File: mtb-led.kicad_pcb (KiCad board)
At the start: 2 copper layers, 120 x 50 mm, 60 parts, among them J7 AVR-ISP-6, J9 DEBUG, SW1 SW_Push, U1 ATmega328PB-A, U2 78M05, U3 TLC5940PWP, U4 TLC5940PWP, U5 MAX487E, Y1 14.7456 MHz

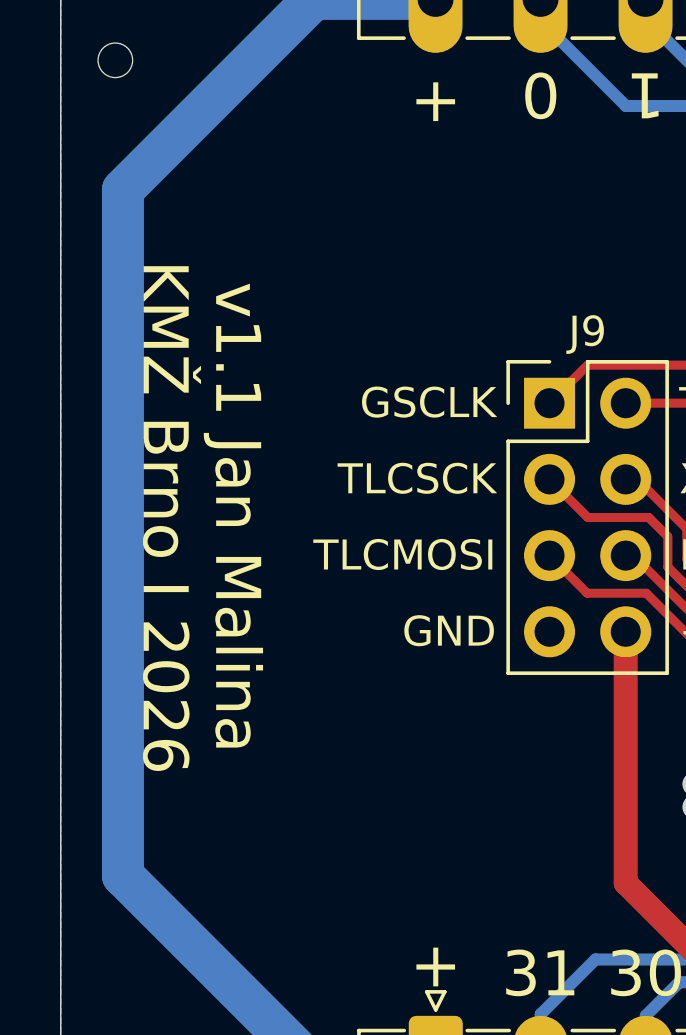
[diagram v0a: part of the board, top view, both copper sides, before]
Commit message: Sch: add I2C interface to ambient light sensor.
E.g. BH1750.
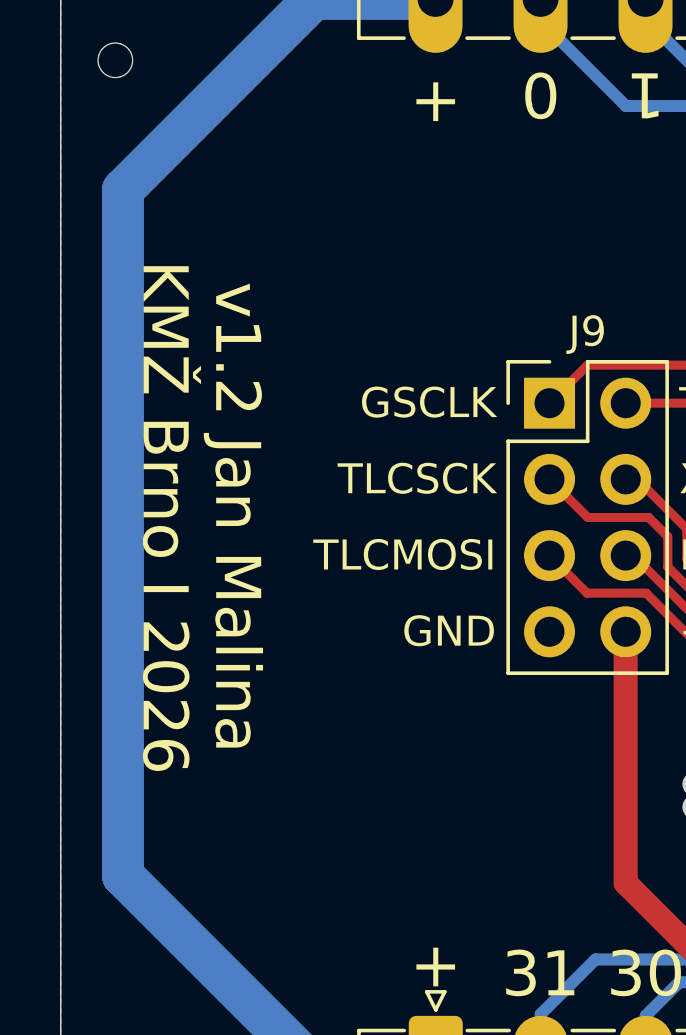
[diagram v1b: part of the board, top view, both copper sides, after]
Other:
- board text added: "v1.2 Jan Malina KMŽ Brno I 2026"
- board text removed: "v1.1 Jan Malina KMŽ Brno I 2026"
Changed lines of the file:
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@@
 		)
 	)
-	(gr_text "v1.1 Jan Malina\nKMŽ Brno I 2026"
+	(gr_text "v1.2 Jan Malina\nKMŽ Brno I 2026"
 		(at 84.582 94.488 270)
 		(layer "F.SilkS")

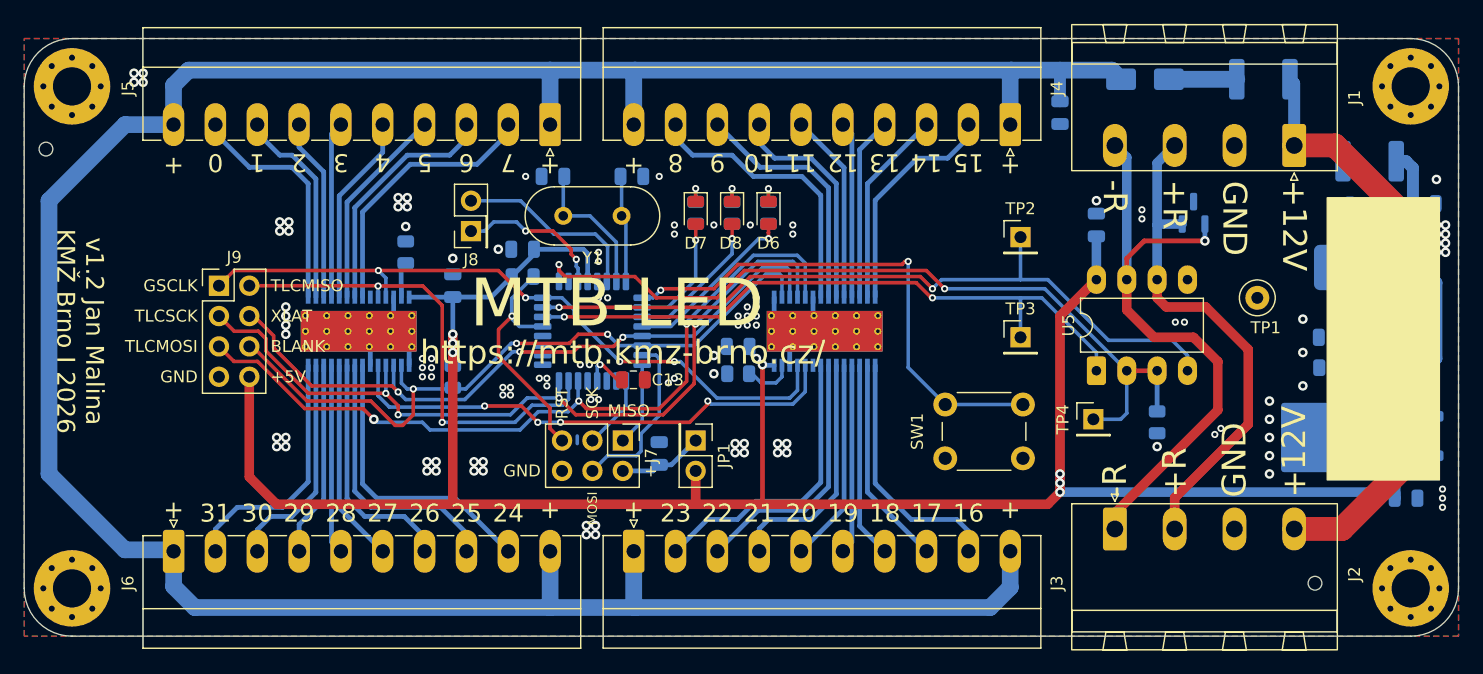
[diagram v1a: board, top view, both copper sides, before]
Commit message: PCB: wire light sensor connection.
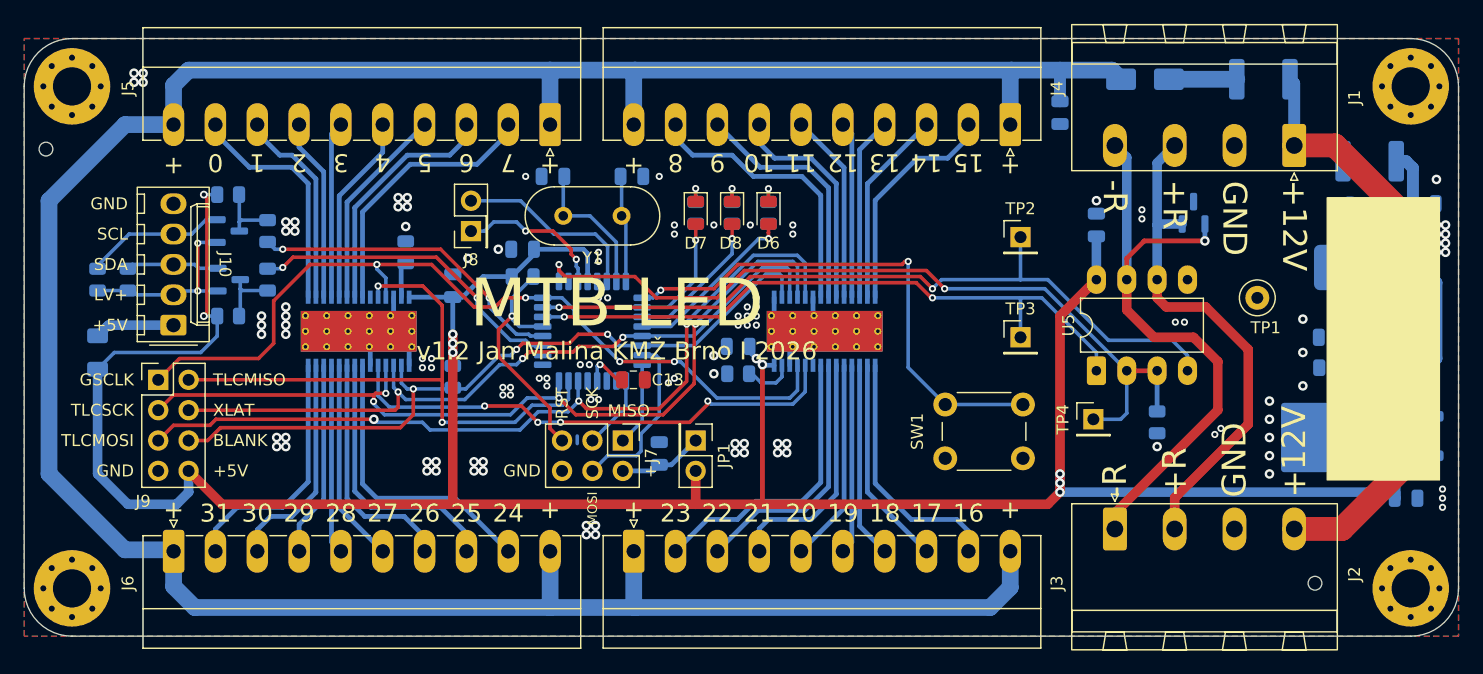
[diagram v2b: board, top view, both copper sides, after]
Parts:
- added F3: 50/100mA, Fuse:Fuse_1206_3216Metric, B.Cu at (88.1, 96.3)
- added J10: KK-254, Connector_Molex:Molex_KK-254_AE-6410-05A_1x05_P2.54mm_Vertical, F.Cu at (94.5, 94.0)
- added Q1: AO3400/BSS138, Package_TO_SOT_SMD:SOT-23, B.Cu at (99.1, 86.1)
- added Q2: AO3400/BSS138, Package_TO_SOT_SMD:SOT-23, B.Cu at (99.1, 90.2)
- added R11: 1k, Resistor_SMD:R_0805_2012Metric, B.Cu at (102.4, 86.1)
- added R12: 10k, Resistor_SMD:R_0805_2012Metric, B.Cu at (99.1, 93.2)
- added R13: 10k, Resistor_SMD:R_0805_2012Metric, B.Cu at (99.1, 83.1)
- added R14: 10k, Resistor_SMD:R_0805_2012Metric, B.Cu at (90.7, 90.2)
- added R15: 10k, Resistor_SMD:R_0805_2012Metric, B.Cu at (88.1, 90.2)
- added R9: 1k, Resistor_SMD:R_0805_2012Metric, B.Cu at (102.4, 90.2)
- JP1: value Jumper_2_Open -> ~
- moved J9 9.37 mm to (93.2, 98.6)
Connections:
- U1 pad 27: unconnected-(U1-PC4-Pad27) -> /SDA
- U1 pad 28: unconnected-(U1-PC5-Pad28) -> /SCL
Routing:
- net +5V: track 195.1 -> 237.0 mm, vias 8 -> 10
- net /SDA: track 0.00 -> 26.9 mm, vias 0 -> 2
- net /SCL: track 0.00 -> 26.8 mm, vias 0 -> 2
- net /LV+: track 0.00 -> 16.2 mm, vias 0 -> 2
- net /GSCLK: track 58.5 -> 70.5 mm
- net /LSCL: track 0.00 -> 11.9 mm
- net /TLCMISO: track 40.4 -> 50.9 mm
- net /LSDA: track 0.00 -> 7.80 mm
- net Net-(J10-Pin_1): track 0.00 -> 6.72 mm
- net Net-(Q1-D): track 0.00 -> 5.49 mm
- net Net-(Q2-D): track 0.00 -> 5.44 mm
- net /TLCSCK: track 68.7 -> 72.1 mm
- net /TLCMOSI: track 66.2 -> 69.5 mm
- net /XLAT: track 58.1 -> 61.2 mm
- net /BLANK: track 59.1 -> 62.0 mm
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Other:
- board text added: "LV+"
- board text added: "SCL"
- board text added: "SDA"
- board text removed: "https://mtb.kmz-brno.cz/"

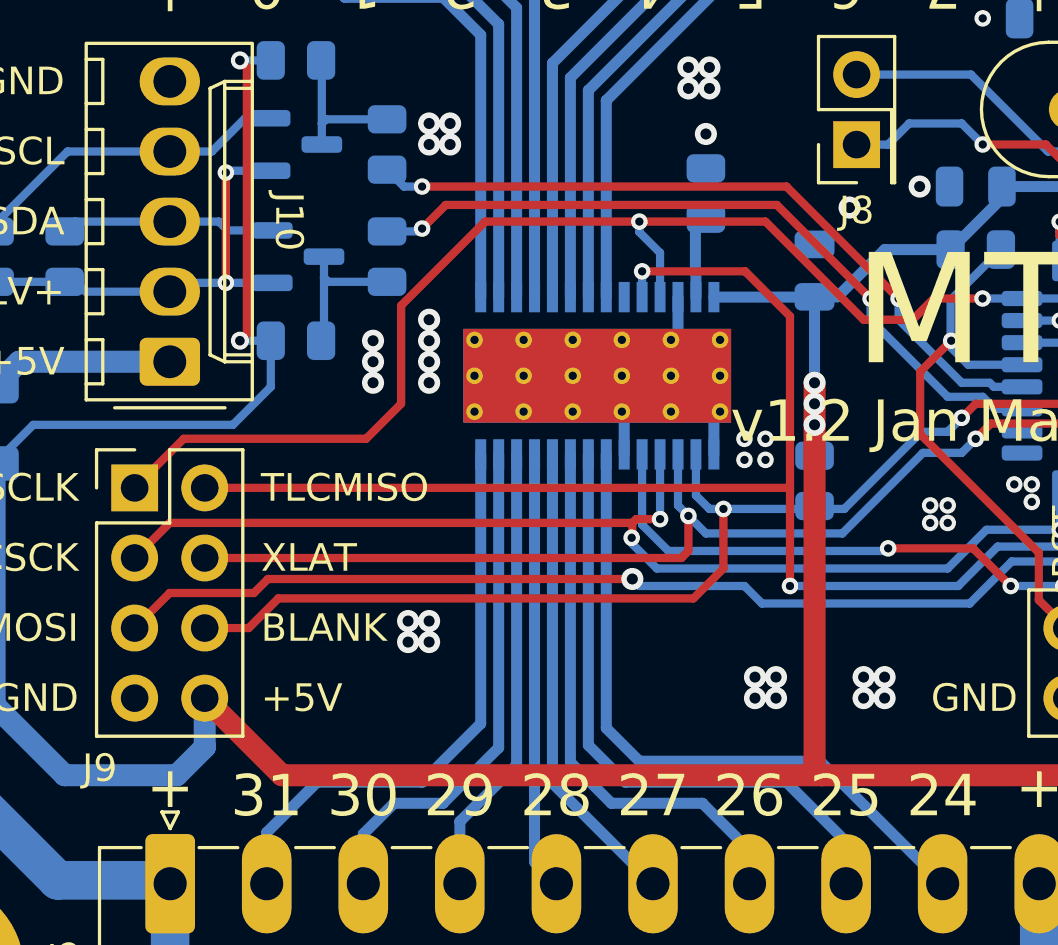
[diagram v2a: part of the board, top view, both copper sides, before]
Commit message: Enhance thermal conductivity from TLC5940.
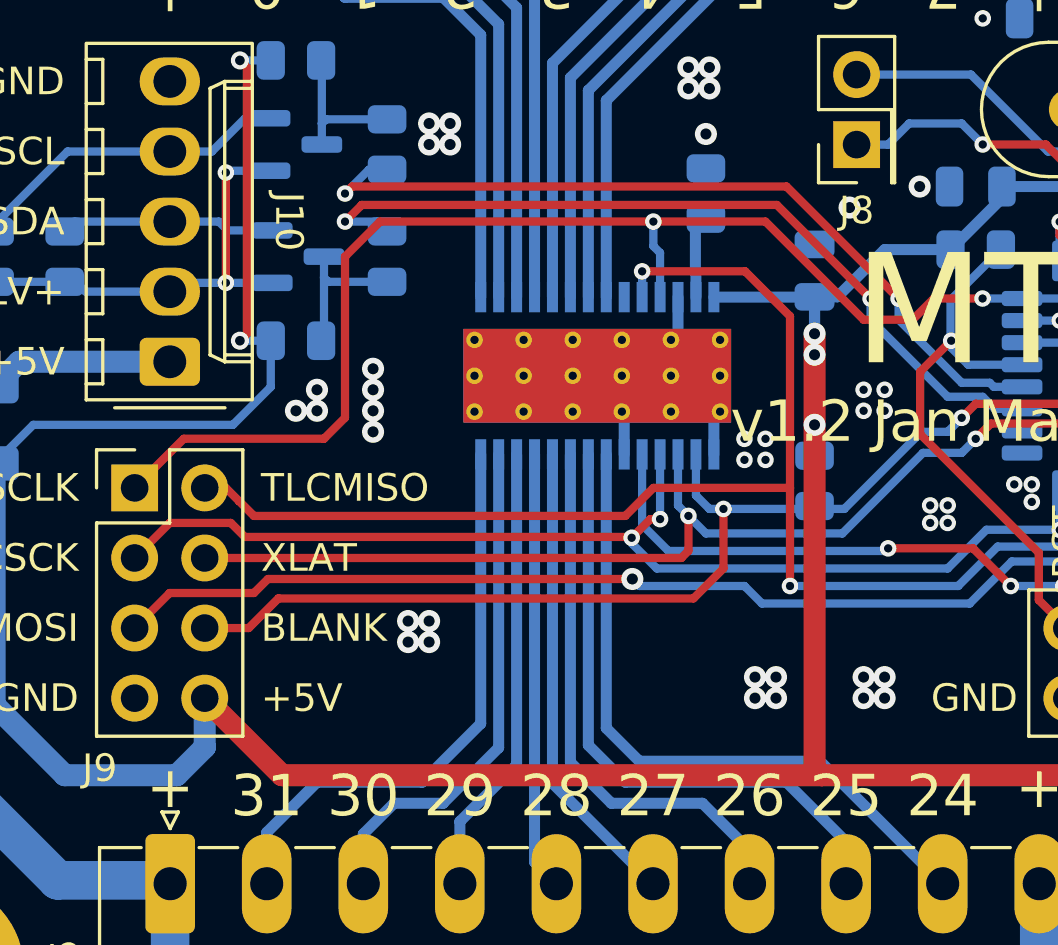
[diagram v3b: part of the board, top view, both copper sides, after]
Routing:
- net /SCL: track 26.8 -> 30.1 mm
- net /SDA: track 26.9 -> 30.0 mm
- net /GSCLK: track 70.5 -> 71.7 mm
- net /TLCMISO: track 50.9 -> 51.7 mm
- net +5V: track 237.0 -> 236.3 mm
- net GND: vias 120 -> 124

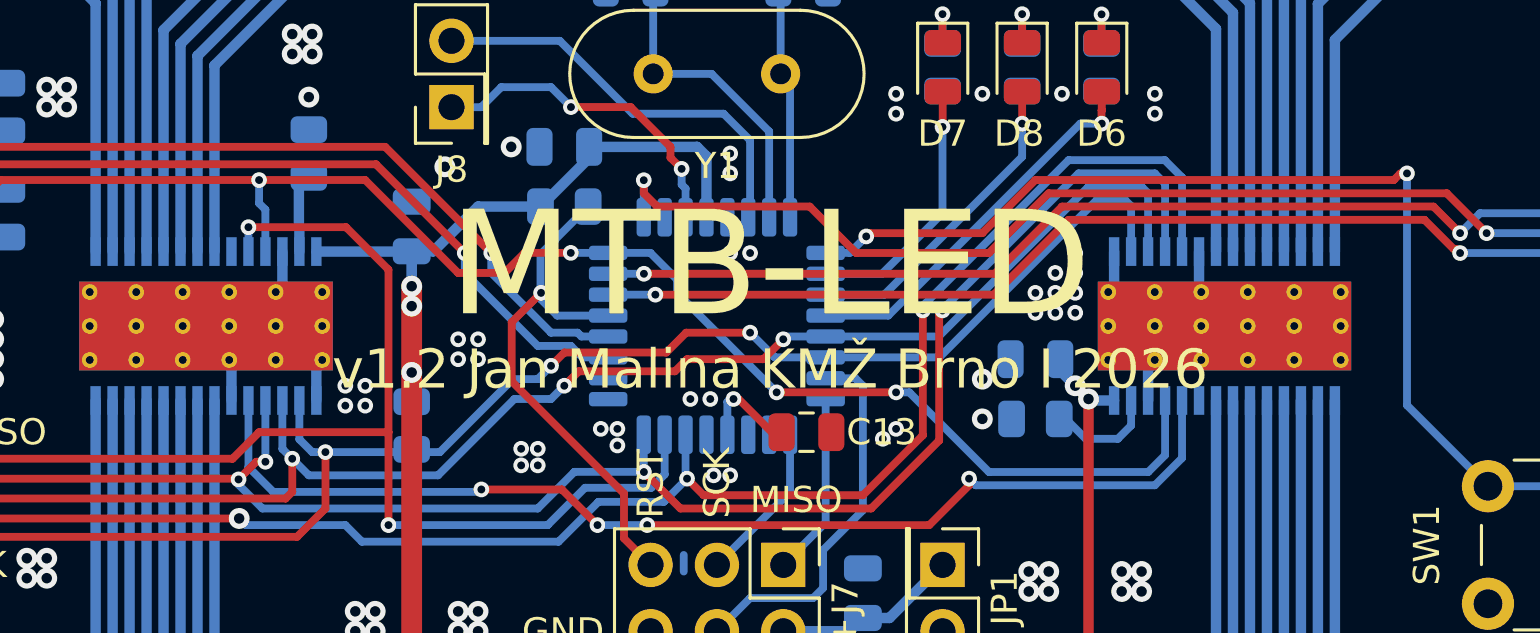
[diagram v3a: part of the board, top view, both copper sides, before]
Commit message: Better thermal connection of TLC5940.
We need to dissipate as max heat as possible.
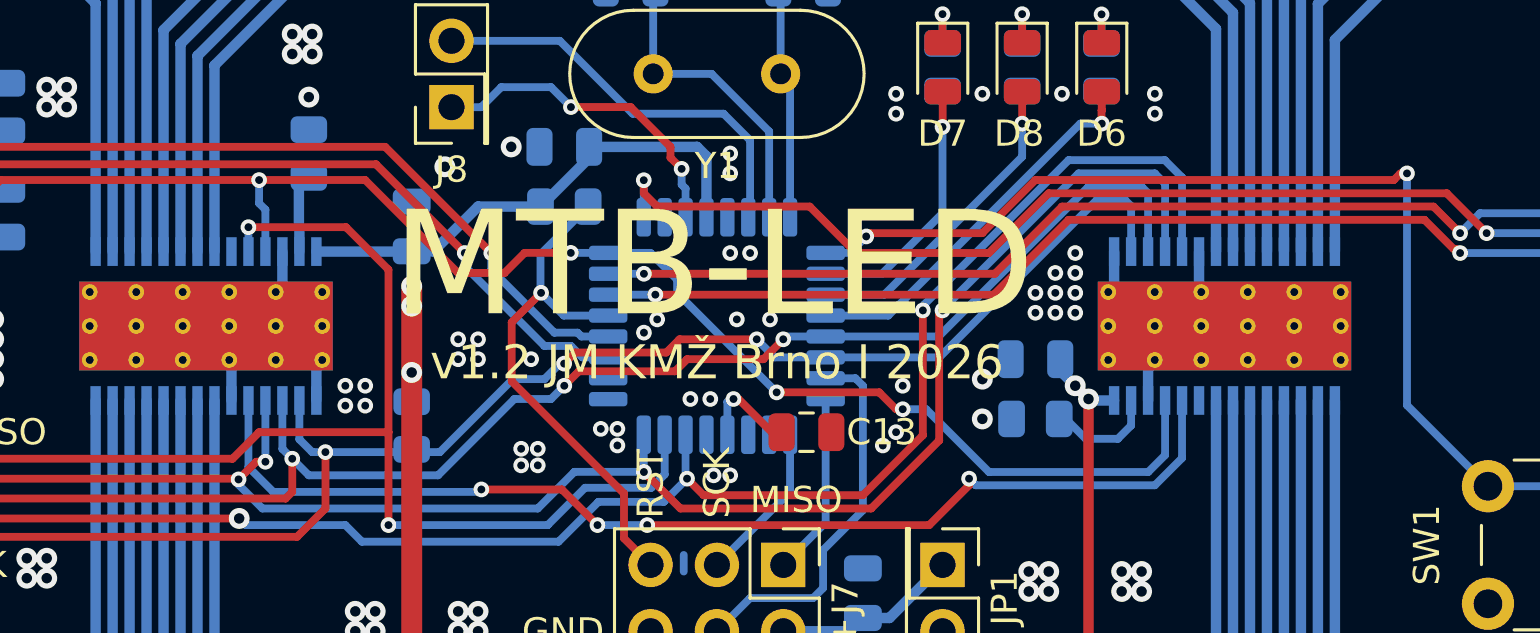
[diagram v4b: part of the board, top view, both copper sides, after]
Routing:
- net GND: vias 124 -> 130
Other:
- board text added: "v1.2 JM KMŽ Brno I 2026"
- board text removed: "v1.2 Jan Malina KMŽ Brno I 2026"
